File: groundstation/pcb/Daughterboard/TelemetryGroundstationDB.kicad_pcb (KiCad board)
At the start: 4 copper layers, 95 x 95 mm, 146 parts, among them J1 USB-C, J2 USB-C, J3 RFPC-SMA28-F, J4 RFPC-SMA28-F, M1 M4 Mounting Hole, M2 M4 Mounting Hole, M3 M4 Mounting Hole, M4 M4 Mounting Hole, Q1 NPN, U1 CP2102N, U2 CP2102N, U3 RC1780HP-RC232, U4 RC1701HP-RC232, U5 AVR128DB64x-xPT, U6 W25Q80DVSSIG

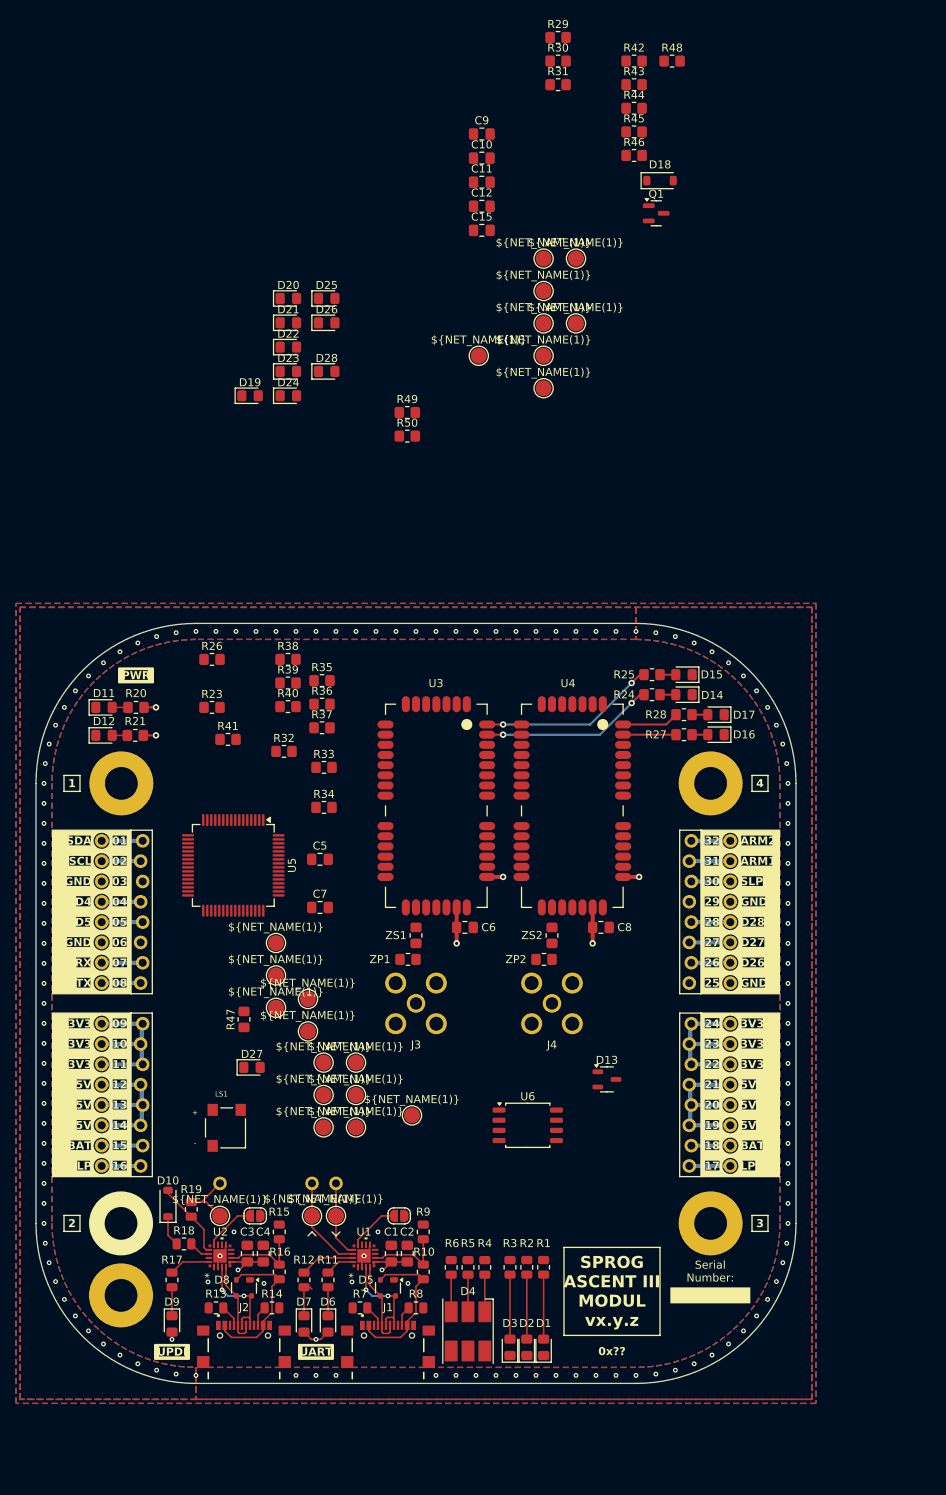
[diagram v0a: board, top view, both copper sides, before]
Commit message: add Daugther board schematic
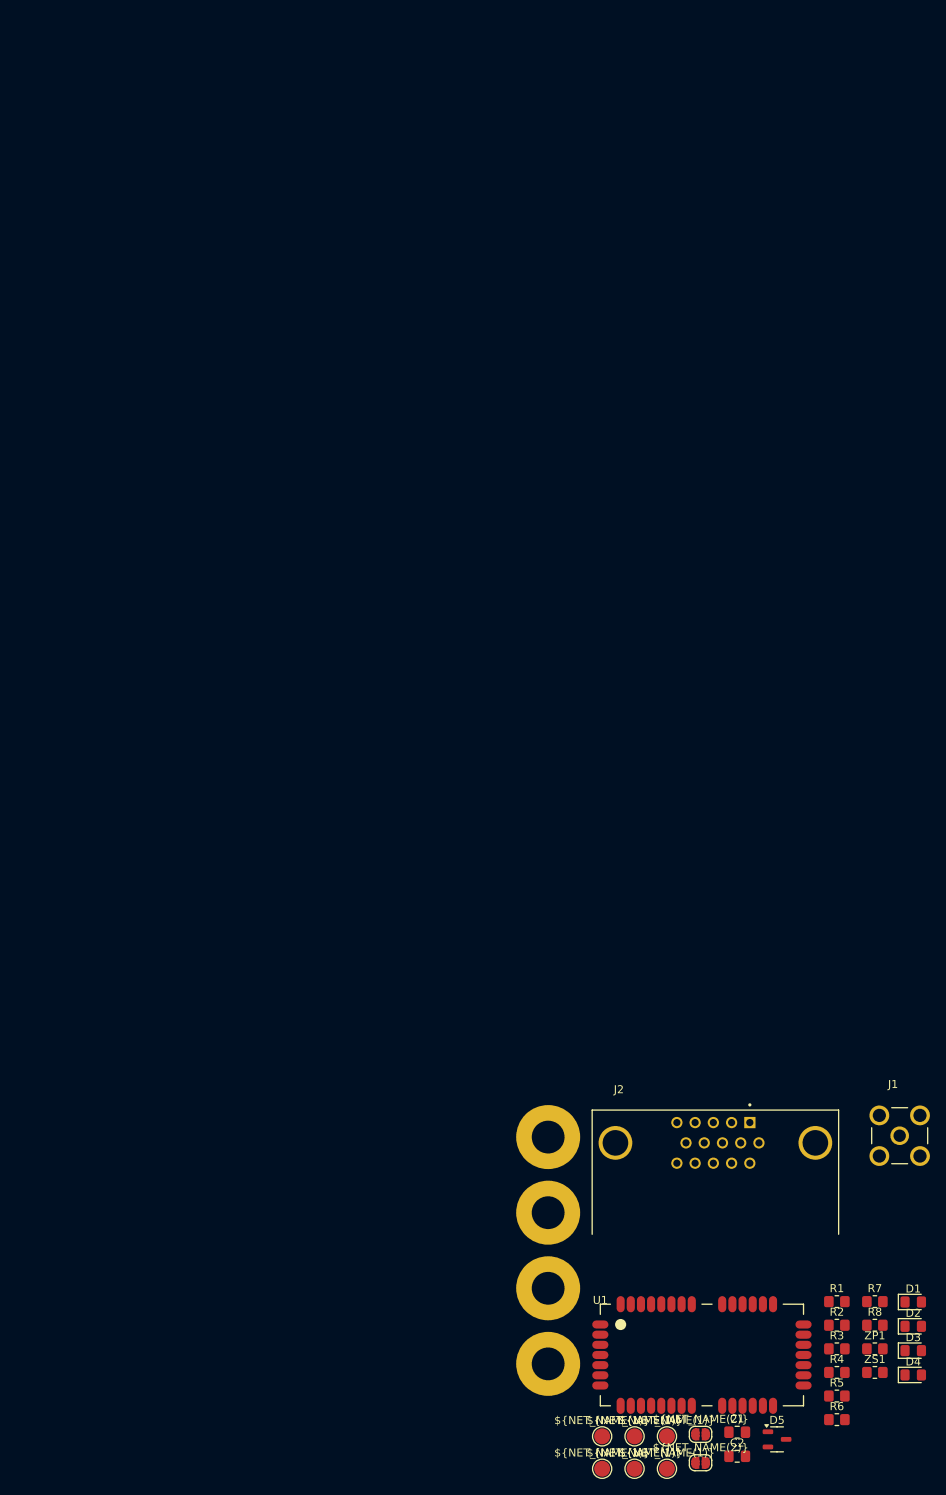
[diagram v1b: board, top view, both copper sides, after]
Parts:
- removed C10, C11, C12, C9: 1 uF, Capacitor_SMD:C_0805_2012Metric_Pad1.18x1.45mm_HandSolder
- removed C15, C6, C8: 1 uf, Capacitor_SMD:C_0805_2012Metric_Pad1.18x1.45mm_HandSolder
- removed C3: 4.7 uF, Capacitor_SMD:C_0805_2012Metric_Pad1.18x1.45mm_HandSolder
- removed C4: 0.1 uF, Capacitor_SMD:C_0805_2012Metric_Pad1.18x1.45mm_HandSolder
- removed C5, C7: 1 nF, Capacitor_SMD:C_0805_2012Metric_Pad1.18x1.45mm_HandSolder
- removed D10: BAT43, Diode_SMD:D_SOD-123
- removed D11, D12, D14, D16, D6: green, LED_SMD:LED_0805_2012Metric_Pad1.15x1.40mm_HandSolder
- removed D13: WE-TVS_SOT23-3L_824021, Package_TO_SOT_SMD:SOT-23-3
- removed D15, D17: yellow, LED_SMD:LED_0805_2012Metric_Pad1.15x1.40mm_HandSolder
- removed D18: D, Diode_SMD:D_SOD-123
- removed D19, D20, D21, D22, D23, D24, D9: red, LED_SMD:LED_0805_2012Metric_Pad1.15x1.40mm_HandSolder
- removed D25, D26, D27, D28, D7: orange, LED_SMD:LED_0805_2012Metric_Pad1.15x1.40mm_HandSolder
- removed D8: SP0503BAHT, Package_TO_SOT_SMD:SOT-143
- removed J3, J4: RFPC-SMA28-F, Footprints:RFPC-SMA28-F
- removed JL1: Stackable Socket 1x8, Footprints:JL1
- removed JL2: Stackable Socket 1x8, Footprints:JL2
- removed JL3: Stackable Socket 1x8, Footprints:JL3
- removed JL4: Stackable Socket 1x8, Footprints:JL4
- removed JR1: Stackable Socket 1x8, Footprints:JR1
- removed JR2: Stackable Socket 1x8, Footprints:JR2
- removed JR3: Stackable Socket 1x8, Footprints:JR3
- removed JR4: Stackable Socket 1x8, Footprints:JR4
- removed LS1: Buzzer CMT-0525-75-SMT-TR, Footprints:Buzzer XDCR_CMT-0525-75-SMT-TR
- removed Q1: NPN, Package_TO_SOT_SMD:SOT-23
- removed R10, R16: 22k, Resistor_SMD:R_0805_2012Metric
- removed R11, R12, R17: 560 Ohm, Resistor_SMD:R_0805_2012Metric
- removed R13, R14: 5k1, Resistor_SMD:R_0805_2012Metric
- removed R15, R9: 47k, Resistor_SMD:R_0805_2012Metric
- removed R18, R19: 470 Ohm, Resistor_SMD:R_0805_2012Metric
- removed R20, R21: 560 Ohm, Resistor_SMD:R_0805_2012Metric_Pad1.20x1.40mm_HandSolder
- removed R23, R26: 2k7, Resistor_SMD:R_0805_2012Metric_Pad1.20x1.40mm_HandSolder
- removed R24, R25, R27, R28: 560R, Resistor_SMD:R_0805_2012Metric_Pad1.20x1.40mm_HandSolder
- removed R29: 180 R, Resistor_SMD:R_0805_2012Metric_Pad1.20x1.40mm_HandSolder
- removed R30, R31, R34, R37, R38, R39, R40, R41, R42, R49, R50: 5k6, Resistor_SMD:R_0805_2012Metric_Pad1.20x1.40mm_HandSolder
- removed R32, R33, R35, R36, R43, R44: 1k, Resistor_SMD:R_0805_2012Metric_Pad1.20x1.40mm_HandSolder
- removed R45, R46, R47, R48: 270R, Resistor_SMD:R_0805_2012Metric_Pad1.20x1.40mm_HandSolder
- removed REF** (x3): Test Point Hole, Footprints:Test Point Hole
- removed TP12, TP13, TP14, TP15, TP16, TP17, TP18, TP19, TP36, TP37, TP38, TP39, TP41, TP60, TP70, TP8, TP80, TP9: TestPoint, Footprints:Test Point
- removed U2: CP2102N, Footprints:QFN20_CP2102N_SIL
- removed U3: RC1780HP-RC232, Footprints:Radiocrafts RC1780HP-RC232
- removed U4: RC1701HP-RC232, Footprints:Radiocrafts RC1780HP-RC232
- removed U5: AVR128DB64x-xPT, Package_QFP:TQFP-64_10x10mm_P0.5mm
- removed U6: W25Q80DVSSIG, Package_SO:SOIC-8_5.3x5.3mm_P1.27mm
- removed ZP2, ZS2: ~, Resistor_SMD:R_0805_2012Metric_Pad1.20x1.40mm_HandSolder
- added TP6: TestPoint, Footprints:Test Point, F.Cu at (32.4, 61.2)
- C1: value 4.7 uF -> 1 nF
- C2: value 0.1 uF -> 1 uf
- D1, D3: value orange -> green
- D2: value orange -> yellow
- D4: value Cree RGB LED -> green; footprint Footprints:Cree RGB LED -> LED_SMD:LED_0805_2012Metric_Pad1.15x1.40mm_HandSolder
- D5: value SP0503BAHT -> WE-TVS_SOT23-3L_824021; footprint Package_TO_SOT_SMD:SOT-143 -> Package_TO_SOT_SMD:SOT-23-3
- J1: value USB-C -> RFPC-SMA27-F; footprint Footprints:GCT_USB4216-03-A_REVA -> Footprints:GRADCONN_RFPC-SMA27-F
- J2: value USB-C -> ICD15S13E4GV00LF; footprint Footprints:GCT_USB4216-03-A_REVA -> Footprints:AMPHENOL_ICD15S13E4GV00LF[1]
- R1: value 560 Ohm -> 2k7; footprint Resistor_SMD:R_0805_2012Metric -> Resistor_SMD:R_0805_2012Metric_Pad1.20x1.40mm_HandSolder
- R2, R3: value 560 Ohm -> 560R; footprint Resistor_SMD:R_0805_2012Metric -> Resistor_SMD:R_0805_2012Metric_Pad1.20x1.40mm_HandSolder
- R4, R5, R6: value 560 Ohm -> 5k6; footprint Resistor_SMD:R_0805_2012Metric -> Resistor_SMD:R_0805_2012Metric_Pad1.20x1.40mm_HandSolder
- R7, R8: value 5k1 -> 560 Ohm; footprint Resistor_SMD:R_0805_2012Metric -> Resistor_SMD:R_0805_2012Metric_Pad1.20x1.40mm_HandSolder
- U1: value CP2102N -> RC1780HP-RC232; footprint Footprints:QFN20_CP2102N_SIL -> Footprints:Radiocrafts RC1780HP-RC232
- moved ZS1 79.2 mm to (58.4, 49.1), turned to 0 degrees
- moved ZP1 76.0 mm to (58.4, 46.2), turned to 0 degrees
- moved M4 75.3 mm to (17.5, 48.1)
- moved J1 69.5 mm to (61.5, 19.5)
- moved M1 69.3 mm to (17.5, 19.7)
- moved J2 64.5 mm to (38.4, 20.4)
- moved R7 64.4 mm to (58.4, 40.3), turned to 0 degrees
- moved TP4 63.9 mm to (28.3, 61.2)
- moved JP2 63.7 mm to (36.6, 60.4)
- moved TP5 60.5 mm to (32.4, 57.1)
- moved TP3 58.7 mm to (28.3, 57.1)
- moved R8 57.4 mm to (58.4, 43.2)
- moved D4 55.9 mm to (63.2, 49.4), turned to 0 degrees
- moved M2 54.4 mm to (17.5, 29.2)
- moved D5 52.2 mm to (46.1, 57.5), turned to 0 degrees
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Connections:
- C1 pad 1: +3V3 -> Net-(U1-RESET)
- D4 pad 1: Net-(D4-AR) -> GND
- D4 pad 2: Net-(D4-AG) -> Net-(D4-A)
- D5 pad 1: GND -> +5V
- D5 pad 2: VBUS1 -> +3V3
- D5 pad 3: D-1 -> GND
- JP1 pad 1: Net-(JP1-A) -> +5V
- JP1 pad 2: GND -> Net-(JP1-B)
- JP2 pad 1: Net-(JP2-A) -> +3V3
- JP2 pad 2: GND -> Net-(JP1-B)
- R1 pad 1: LED 1 -> Net-(U1-RESET)
- R1 pad 2: Net-(D1-A) -> RST
- R2 pad 1: LED 2 -> Net-(D1-A)
- R2 pad 2: Net-(D2-A) -> Net-(U1-D1)
- R3 pad 1: LED 3 -> Net-(D2-A)
- R3 pad 2: Net-(D3-A) -> Net-(U1-D2)
- R4 pad 1: LED R -> CFG
- R4 pad 2: Net-(D4-AR) -> +3V3
- R5 pad 1: LED G -> RST
- R5 pad 2: Net-(D4-AG) -> +3V3
- R6 pad 1: LED B -> TX
- R6 pad 2: Net-(D4-AB) -> +3V3
- R7 pad 1: Net-(J1-CC1) -> +3V3
- R7 pad 2: GND -> Net-(D3-A)
- R8 pad 1: Net-(J1-CC2) -> +5V
- R8 pad 2: GND -> Net-(D4-A)
- TP1 pad 1: RX4 -> TX
- TP2 pad 1: TX4 -> RX
- TP3 pad 1: UPDI -> RST
- TP4 pad 1: CTS1 -> CTS
- TP5 pad 1: CFG1 -> CFG
- U1 pad 1: unconnected-(U1-RS485/GPIO.1-Pad1) -> GND
- U1 pad 10: unconnected-(U1-NC-Pad10) -> GND
- U1 pad 12: GND -> Net-(U1-RESET)
- U1 pad 13: unconnected-(U1-~{WAKEUP}-Pad13) -> +3V3
- U1 pad 14: unconnected-(U1-SUSPEND-Pad14) -> GND
- U1 pad 15: Net-(JP1-A) -> unconnected-(U1-Pad15)
- U1 pad 17: TX4 -> unconnected-(U1-Pad17)
- U1 pad 18: RX4 -> unconnected-(U1-Pad18)
- U1 pad 19: Net-(U1-~{RXT}/GPIO.3) -> unconnected-(U1-DD-Pad19)
- U1 pad 2: unconnected-(U1-CLK/GPIO.0-Pad2) -> CTS
- U1 pad 20: Net-(U1-~{TXT}/GPIO.2) -> unconnected-(U1-DC-Pad20)
- U1 pad 21: GND -> unconnected-(U1-Pad21)
- U1 pad 3: GND -> RTS
- U1 pad 4: D+1 -> CFG
- U1 pad 5: D-1 -> RX
- U1 pad 6: +3V3 -> TX
- U1 pad 7: +3V3 -> GND
- U1 pad 8: Net-(U1-VBUS) -> GND
- U1 pad 9: unconnected-(U1-~{RST}-Pad9) -> Net-(U1-RF)
- ZP1 pad 1: Net-(J3-Pad1) -> Net-(J1-Pad1)
- ZS1 pad 1: Net-(U3-RF) -> Net-(U1-RF)
- ZS1 pad 2: Net-(J3-Pad1) -> Net-(J1-Pad1)
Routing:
- net +3V3: track 67.6 -> 0.00 mm, vias 8 -> 0
- net +5V: track 41.7 -> 0.00 mm, vias 2 -> 0
- net Net-(U3-D2): track 22.2 -> 0.00 mm, vias 2 -> 0
- net Net-(U3-D1): track 21.7 -> 0.00 mm, vias 2 -> 0
- net VBUS2: track 19.3 -> 0.00 mm
- net VBUS1: track 19.3 -> 0.00 mm
- net D+2: track 12.6 -> 0.00 mm, vias 2 -> 0
- net D+1: track 12.6 -> 0.00 mm, vias 2 -> 0
- net RX: track 12.0 -> 0.00 mm
- net D-2: track 10.7 -> 0.00 mm
- net D-1: track 10.7 -> 0.00 mm
- net Net-(U1-VBUS): track 10.5 -> 0.00 mm
- net Net-(D10-A): track 10.1 -> 0.00 mm
- net +V_BATT: track 10.0 -> 0.00 mm
- net +3V_LP: track 10.0 -> 0.00 mm
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- removed copper zone on In2.Cu, net +3V3
- removed copper zone on B.Cu, net GND
- removed copper zone on F.Cu, net GND
- removed copper zone on In1.Cu, net GND
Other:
- board outline removed
- copper layers 4 -> 2
- board text removed: "01"
- board text removed: "02"
- board text removed: "03"
- board text removed: "04"
- board text removed: "05"
- board text removed: "06"
- board text removed: "07"
- board text removed: "08"
- board text removed: "09"
- board text removed: "0x??"
- board text removed: "1"
- board text removed: "10"
- board text removed: "11"
- board text removed: "12"
- board text removed: "13"
- board text removed: "14"
- board text removed: "15"
- board text removed: "16"
- board text removed: "17"
- board text removed: "18"
- board text removed: "19"
- board text removed: "2"
- board text removed: "20"
- board text removed: "21"
- board text removed: "22"
- board text removed: "23"
- board text removed: "24"
- board text removed: "25"
- board text removed: "26"
- board text removed: "27"
- board text removed: "28"
- board text removed: "29"
- board text removed: "3"
- board text removed: "30"
- board text removed: "31"
- board text removed: "32"
- board text removed: "3V3"
- board text removed: "4"
- board text removed: "5V"
- board text removed: "ARM1"
- board text removed: "ARM2"
- board text removed: "BAT"
- board text removed: "D26"
- board text removed: "D27"
- board text removed: "D28"
- board text removed: "D4"
- board text removed: "D5"
- board text removed: "GND"
- board text removed: "LP"
- board text removed: "PWR"
- board text removed: "RX"
- board text removed: "SCL"
- board text removed: "SDA"
- board text removed: "SLP"
- board text removed: "SPACEFLIGHT ROCKETRY GIESSEN"
- board text removed: "SPROG ASCENT III MODUL vx.y.z"
- board text removed: "Serial Number:"
- board text removed: "TX"
- board text removed: "UART"
- board text removed: "UPDI"

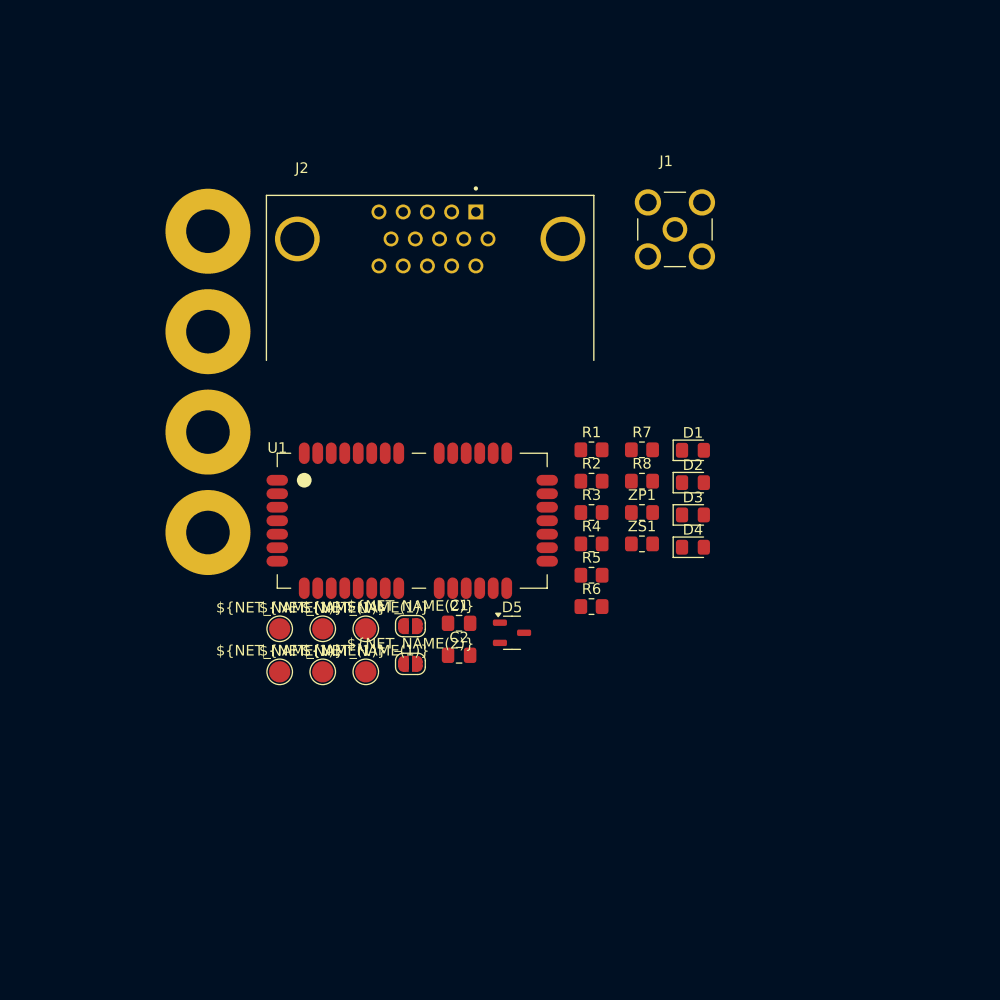
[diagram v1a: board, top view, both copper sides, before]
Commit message: small change to Daughterboard schematic + pcb
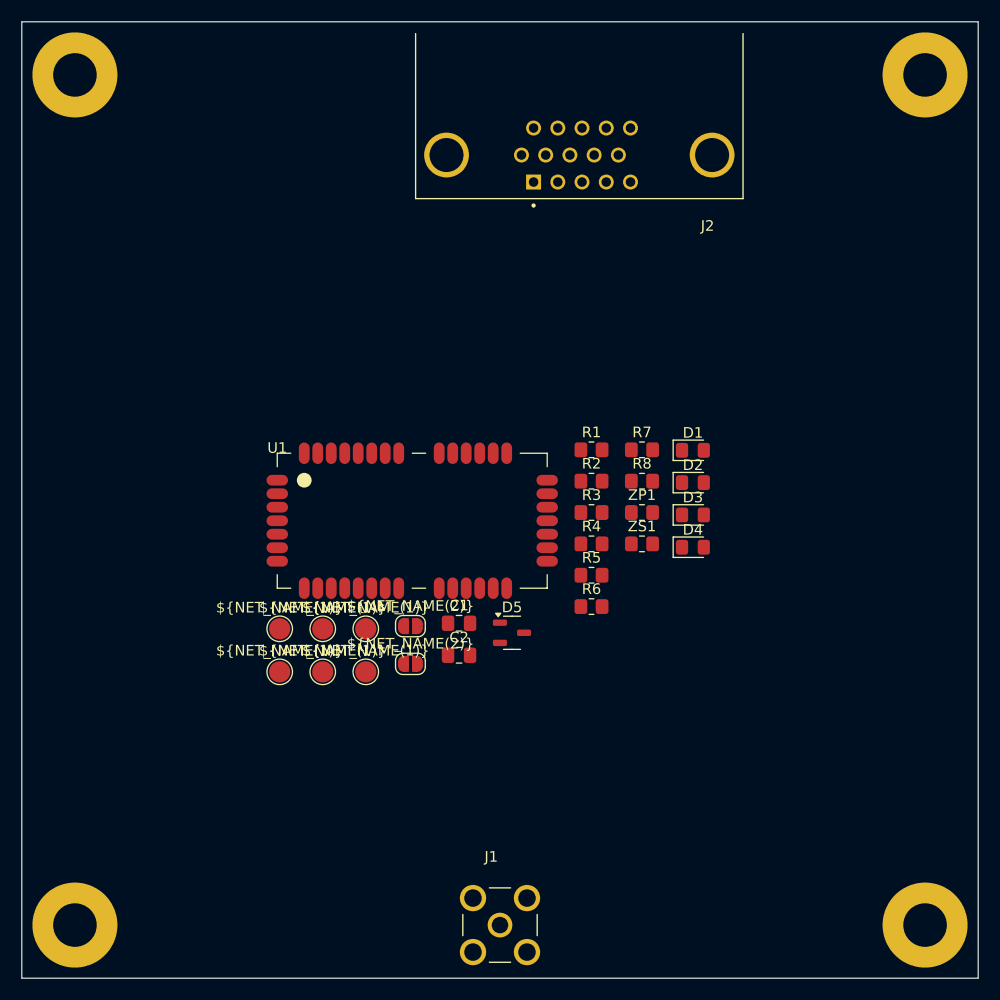
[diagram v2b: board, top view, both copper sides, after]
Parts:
- moved M1 93.9 mm to (85.0, 85.0)
- moved M2 71.7 mm to (85.0, 5.00)
- moved J1 67.5 mm to (45.0, 85.0)
- moved M4 39.0 mm to (5.00, 85.0)
- moved M3 35.9 mm to (5.00, 5.00)
- moved J2 16.1 mm to (52.5, 12.5), turned to 180 degrees
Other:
- board outline added: 90 x 90 mm
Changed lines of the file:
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@@
 	(footprint "Footprints:M4 Mounting Hole"
 		(layer "F.Cu")
-		(at 17.52 38.61)
+		(at 5 5)
 		(property "Reference" "M3"
 			(at 0 -0.5 0)
@@
 	(footprint "Footprints:M4 Mounting Hole"
 		(layer "F.Cu")
-		(at 17.52 19.71)
+		(at 85 85)
 		(property "Reference" "M1"
 			(at 0 -0.5 0)
@@
 	(footprint "Footprints:M4 Mounting Hole"
 		(layer "F.Cu")
-		(at 17.52 48.06)
+		(at 5 85)
 		(property "Reference" "M4"
 			(at 0 -0.5 0)
@@
 	(footprint "Footprints:AMPHENOL_ICD15S13E4GV00LF[1]"
 		(layer "F.Cu")
-		(at 38.425 20.435)
+		(at 52.465 12.54 180)
 		(property "Reference" "J2"
 			(at -12.065 -6.6675 0)
@@
 		(attr through_hole)
 		(fp_line
-			(start -15.405 -4.1)
-			(end 15.405 -4.1)
+			(start 15.405 -4.1)
+			(end 15.405 11.43)
 			(stroke
 				(width 0.127)
@@
 		)
 		(fp_line
-			(start 15.405 -4.1)
-			(end 15.405 11.43)
+			(start -15.405 -4.1)
+			(end 15.405 -4.1)
 			(stroke
 				(width 0.127)
@@
 		)
 		(fp_line
-			(start -15.655 -4.35)
-			(end -15.655 17.85)
+			(start 15.655 17.85)
+			(end 15.655 -4.35)
 			(stroke
 				(width 0.05)
@@
 		)
 		(fp_line
-			(start -15.655 17.85)
-			(end 15.655 17.85)
+			(start 15.655 -4.35)
+			(end -15.655 -4.35)
 			(stroke
 				(width 0.05)
@@
 		)
 		(fp_line
-			(start 15.655 -4.35)
-			(end -15.655 -4.35)
+			(start -15.655 17.85)
+			(end 15.655 17.85)
 			(stroke
 				(width 0.05)
@@
 		)
 		(fp_line
-			(start 15.655 17.85)
-			(end 15.655 -4.35)
+			(start -15.655 -4.35)
+			(end -15.655 17.85)
 			(stroke
 				(width 0.05)
@@
 		)
 		(fp_line
-			(start -15.405 -4.1)
-			(end 15.405 -4.1)
+			(start 17.92 11.43)
+			(end -15.405 11.43)
 			(stroke
 				(width 0.127)
@@
 		)
 		(fp_line
-			(start -15.405 11.43)
-			(end -15.405 -4.1)
+			(start 15.405 17.6)
+			(end -15.405 17.6)
 			(stroke
 				(width 0.127)
@@
 		)
 		(fp_line
-			(start -15.405 17.6)
-			(end -15.405 11.43)
+			(start 15.405 -4.1)
+			(end 15.405 17.6)
 			(stroke
 				(width 0.127)
@@
 		)
 		(fp_line
-			(start 15.405 -4.1)
-			(end 15.405 17.6)
+			(start -15.405 17.6)
+			(end -15.405 11.43)
 			(stroke
 				(width 0.127)
@@
 		)
 		(fp_line
-			(start 15.405 17.6)
-			(end -15.405 17.6)
+			(start -15.405 11.43)
+			(end -15.405 -4.1)
 			(stroke
 				(width 0.127)
@@
 		)
 		(fp_line
-			(start 17.92 11.43)
-			(end -15.405 11.43)
+			(start -15.405 -4.1)
+			(end 15.405 -4.1)
 			(stroke
 				(width 0.127)
@@
 		)
 		(pad "1" thru_hole rect
-			(at 4.305 -2.54)
+			(at 4.305 -2.54 180)
 			(size 1.408 1.408)
 			(drill 0.9)
@@
 		)
 		(pad "2" thru_hole circle
-			(at 2.025 -2.54)
+			(at 2.025 -2.54 180)
 			(size 1.408 1.408)
 			(drill 0.9)
@@
 		)
 		(pad "3" thru_hole circle
-			(at -0.255 -2.54)
+			(at -0.255 -2.54 180)
 			(size 1.408 1.408)
 			(drill 0.9)
@@
 		)
 		(pad "4" thru_hole circle
-			(at -2.535 -2.54)
+			(at -2.535 -2.54 180)
 			(size 1.408 1.408)
 			(drill 0.9)
@@
 		)
 		(pad "5" thru_hole circle
-			(at -4.815 -2.54)
+			(at -4.815 -2.54 180)
 			(size 1.408 1.408)
 			(drill 0.9)
@@
 		)
 		(pad "6" thru_hole circle
-			(at 5.445 0)
+			(at 5.445 0 180)
 			(size 1.408 1.408)
 			(drill 0.9)
@@
 		)
 		(pad "7" thru_hole circle
-			(at 3.165 0)
+			(at 3.165 0 180)
 			(size 1.408 1.408)
 			(drill 0.9)
@@
 		)
 		(pad "8" thru_hole circle
-			(at 0.885 0)
+			(at 0.885 0 180)
 			(size 1.408 1.408)
 			(drill 0.9)
@@
 		)
 		(pad "9" thru_hole circle
-			(at -1.395 0)
+			(at -1.395 0 180)
 			(size 1.408 1.408)
 			(drill 0.9)
@@
 		)
 		(pad "10" thru_hole circle
-			(at -3.675 0)
+			(at -3.675 0 180)
 			(size 1.408 1.408)
 			(drill 0.9)
@@
 		)
 		(pad "11" thru_hole circle
-			(at 4.305 2.54)
+			(at 4.305 2.54 180)
 			(size 1.408 1.408)
 			(drill 0.9)
@@
 		)
 		(pad "12" thru_hole circle
-			(at 2.025 2.54)
+			(at 2.025 2.54 180)
 			(size 1.408 1.408)
 			(drill 0.9)
@@
 		)
 		(pad "13" thru_hole circle
-			(at -0.255 2.54)
+			(at -0.255 2.54 180)
 			(size 1.408 1.408)
 			(drill 0.9)
@@
 		)
 		(pad "14" thru_hole circle
-			(at -2.535 2.54)
+			(at -2.535 2.54 180)
 			(size 1.408 1.408)
 			(drill 0.9)
@@
 		)
 		(pad "15" thru_hole circle
-			(at -4.815 2.54)
+			(at -4.815 2.54 180)
 			(size 1.408 1.408)
 			(drill 0.9)
@@
 		)
 		(pad "SH1" thru_hole circle
-			(at -12.495 0)
+			(at -12.495 0 180)
 			(size 4.216 4.216)
 			(drill 3.2)
@@
 		)
 		(pad "SH2" thru_hole circle
-			(at 12.495 0)
+			(at 12.495 0 180)
 			(size 4.216 4.216)
 			(drill 3.2)
@@
 	(footprint "Footprints:M4 Mounting Hole"
 		(layer "F.Cu")
-		(at 17.52 29.16)
+		(at 85 5)
 		(property "Reference" "M2"
 			(at 0 -0.5 0)
@@
 	(footprint "Footprints:GRADCONN_RFPC-SMA27-F"
 		(layer "F.Cu")
-		(at 61.46 19.54)
+		(at 45 85)
 		(property "Reference" "J1"
 			(at -0.825 -6.425 0)
@@
 		)
 	)
+	(gr_rect
+		(start 0 0)
+		(end 90 90)
+		(stroke
+			(width 0.1)
+			(type default)
+		)
+		(fill no)
+		(layer "Edge.Cuts")
+	)
 	(embedded_fonts no)
